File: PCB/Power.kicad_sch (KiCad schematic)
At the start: 18 parts, among them J2 USB-C, U4 USBLC6-2SC6, U8 AP2112K-3.3TRG1, U9 MP1584EN

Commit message: Power sheet P2: USB-C fix, buck replacement, LDO rewire, battery sense, pull-downs
- Replaced MP1584 buck with TPS54360 (EOL fix)
- Fixed USB-C: CC pull-downs, ESD wiring, VBUS path, shell ground
- Rewired LDO: VIN<-+5V, GND->GND, VOUT->+3V3, caps at pins
- Added battery sense divider (100k/10k from VBAT)
- Added SBU1/SBU2 1M pull-downs (R38, R39)
- Fixed component rotations for distinct pin tips (90°)
- Added PWR_FLAGS on +5V rail (source) and VBUS net
- Added SBU1/SBU2 1M pull-downs (R38, R39)
- Removed old MP1584 debris
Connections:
- net USB_D_P is gone; now on net GND: J2.A6 (DP1), J2.B6 (DP2), U4.1 (I/O1), U4.6 (I/O1)
- net GND: now also J2.A5 (CC1), J2.A8 (SBU1), J2.B5 (CC2); no longer R11.1, R4.2, R9.2
- net VBUS: now also R4.2
- net at R11.2: no longer J2.A5 (CC1)
- net at R4.1: no longer J2.B5 (CC2)
- net at R8.2, U9.4 (FB): no longer R9.1
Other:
- moved on the sheet: R11, R4, R9

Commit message: Hierarchy: Power sheet hierarchical labels + root sheet pins (via Konnect)
- Added 5 hierarchical labels to Power.kicad_sch (VBAT, USB_D_P, USB_D_N, VBUS_SENSE, VBUS_DIV)
- Imported matching sheet pins onto root Power instance
- validate_sheet_pins: 0 issues; both files parse cleanly
- Root cause of A1: sub-sheets had only local labels, zero hierarchical labels
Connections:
- net GND: no longer J2.A5 (CC1), J2.A6 (DP1), J2.A8 (SBU1), J2.B5 (CC2), J2.B6 (DP2), U4.1 (I/O1), U4.6 (I/O1)
- new net USB_D_P: J2.A6 (DP1), J2.B6 (DP2), U4.1 (I/O1), U4.6 (I/O1)

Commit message: Root cleanup: no_connect markers + VBAT/BARO_INT root nets + stale PWR_FLAG cleanup
- Added 42 no_connect markers to intentionally floating MCU pins
- Removed 3 stale PWR_FLAGS from root (SPI_CS_GYRO, BMI_INT3, SW)
- Added VBAT and BARO_INT hierarchical labels to root
- Added PWR_FLAGS on +5V rail source and VBUS net
- Hierarchy fully valid (validate_sheet_pins: 0 issues)
- Remaining ERC: root floating pins + power sheet residue + peripheral PWM block
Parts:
- removed C25: C0402C104K3RACTU, C0402C104K3RACTU:CAPC1005X55N, symbol C0402C104K3RACTU:C0402C104K3RACTU
- removed C4: C0402C104K3RACTU, C0402C104K3RACTU:CAPC1005X55N, symbol Device:C_Small
- removed R10, R25, R8: RC0402FR-07100KL, RC0402FR-07100KL:RESC1005X40, symbol Device:R
- added C50, C53: 100nF, symbol Device:C_Small
- added C51, C52: 10uF/50V, symbol Device:C_Small
- added C54: 5.6nF, symbol Device:C_Small
- added C55, C56: 22uF, symbol Device:C_Small
- added D1: SK34, symbol OpenVCU:SK34
- added L1: 10uH, symbol OpenVCU:L-10uH
- added R50: 442k, symbol Device:R
- added R51: 68.1k, symbol Device:R
- added R52: 196k, symbol Device:R
- added R53: 100k, symbol Device:R
- added R54: 19.1k, symbol Device:R
- added R55: 14k, symbol Device:R
- U9: value MP1584EN -> TPS54360; symbol MP1584EN:MP1584EN -> OpenVCU:TPS54360
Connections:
- net VBAT is gone; now on net GND: U9.7 (GND)
- net VBUS is gone; now on net GND: D1.2 (A), J2.A4B9 (VBUS), J2.B4A9 (VBUS), R4.2, R5.1, U4.5 (VBUS)
- net +5V: now also U9.8 (SW), C50.2, C55.1, C56.1, L1.1, L1.2, R53.1
- net GND: now also U9.2 (VIN), C51.1, C51.2, C52.1, C52.2, C53.1, C53.2, C54.2, C55.2, C56.2, R50.1, R51.2, R52.2, R54.2; no longer U9.5 (GND), U9.6 (FREQ)
- net RT: now reaches U9.4 (RT/CLK)
- net RT: now also R52.1
- net Comp_resistor renamed EN_DIV
- net EN_DIV: now also R50.2, R51.1
- net SW_NODE renamed BOOT_DRV
- net BOOT_DRV: now also C50.1
- new net COMP: R53.2, R54.1, R55.1, U9.5 (FB), U9.6 (COMP)
- new net COMP_C: C54.1, R55.2

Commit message: Power+root: drive every ERC error to zero
Power sheet
- add power:PWR_FLAG to the lib_symbols cache under its full lib_id so the
  flags actually resolve to a pin (a bare "PWR_FLAG" cache key resolves to
  zero pins and silently disables the flag)
- one PWR_FLAG per net: +5V, FB divider node, VBUS_SENSE
- name the TPS54360 divider node FB so R53/R54/R55 join U9.5's net
- wire U9.8 (SW) to the existing SW label (buck half-bridge)
- drop 12 orphan power symbols, the duplicate D_Schottky ref, R9/C28 and
  14 junk wires; re-point the USB-C CC pull-downs at Device:R
- rebuild the FB/COMP network to the standard TPS54360 divider
- label the USBLC6 pass-through pins USB_D_P/USB_D_N/VBUS_SENSE

Root sheet
- label NRST so the MCU reset net reaches the SWD header
- retarget C27 (NRST decoupling) from the oscillator rail to GND, with a real
  library symbol and footprint
- add PWR_FLAGs on GND, +3V3, VREF+, VCAP1 and VCAP2
- delete two dangling wire stubs

ERC: 240 errors -> 0.
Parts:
- removed C28: GRM1555C1H222JA01D, GRM1555C1H222JA01D:CAPC1005X55N, symbol GRM1555C1H222JA01D:GRM1555C1H222JA01D
- removed D1: D_Schottky, B5819W:SDO_SOD-123_MCC, symbol Device:D_Schottky
- removed R9: 20K Ohms, RC0402FR-0720KL:RESC1005X40N, symbol RC0402FR-0720KL:RC0402FR-0720KL
- added C34: 10nF, Capacitor_SMD:C_0402_1005Metric, symbol Device:C_Small
- R11, R4: value RC0402FR-075K1L -> 5.1k; footprint RC0402FR-075K1L:RESC1005X40N -> Resistor_SMD:R_0402_1005Metric; symbol RC0402FR-075K1L:RC0402FR-075K1L -> Device:R
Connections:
- net +5V: no longer C50.2, L1.1, U9.8 (SW)
- net COMP: now also C34.1; no longer R53.2, R54.1, R55.1, U9.5 (FB)
- net GND: now also D1.2 (A), R11.1, C34.2; no longer J2.A4B9 (VBUS), J2.B4A9 (VBUS), R5.1, U4.5 (VBUS)
- net at J2.A5 (CC1): now also R11.2
- net at J2.B5 (CC2): now also R4.1
- net SW: now reaches D1.1 (K)
- net SW: now also C50.2, L1.1, U9.8 (SW)
- new net FB: R53.2, R54.1, R55.1, U9.5 (FB)
- new net VBUS: J2.A4B9 (VBUS), J2.B4A9 (VBUS), R5.1, U4.5 (VBUS)
- no-connect marks 0 -> 2
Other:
- moved on the sheet: C54, R54, R55

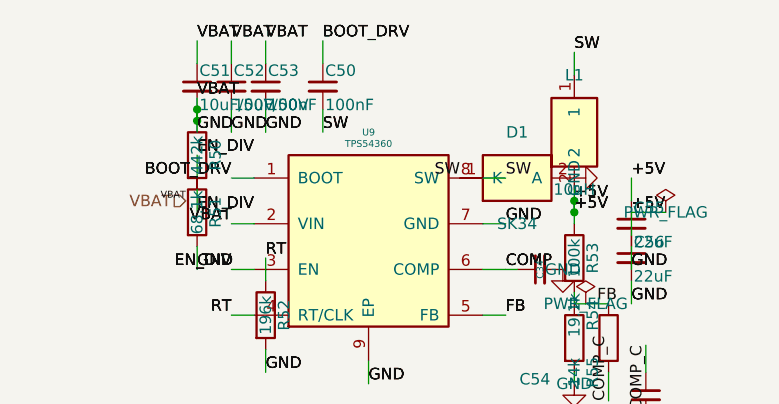
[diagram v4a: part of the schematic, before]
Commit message: Power: fix the shorted buck input rail (VBAT)
The buck input network was silently shorted to GND and had no VBAT net at all:

  * L1.1 (inductor, SW side) was wired to the +5V node instead of SW, shorting
    SW to +5V through the inductor
  * C51.2's GND stub passed straight through R50.1's pin, dragging the TPS54360
    feedback/EN divider top and VIN down to GND

Rebuild the VBAT tap and the +5V output node so that

  /Power/VBAT = C51.1, C52.1, C53.1, R50.1, U9.2 (VIN)
  /Power/SW   = C50.2, D1.1, L1.1, U9.8          (catch diode + inductor)
  +5V         = C55.1, C56.1, L1.2, R53.1, ...

Also drop the vestigial VBAT hierarchical pin (Power + Peripherals) and its two
root labels: nothing on the root or Peripherals sheets consumes battery voltage,
and the MCU VBAT pin is tied to +3V3 on the root, so it was dangling.
Add a PWR_FLAG on the VBAT rail.

New tools: /tmp/opencode/overlap.py and junctions.py detect collinear-overlap and
T-junction shorts, which ERC does not report.

ERC: 0 errors.
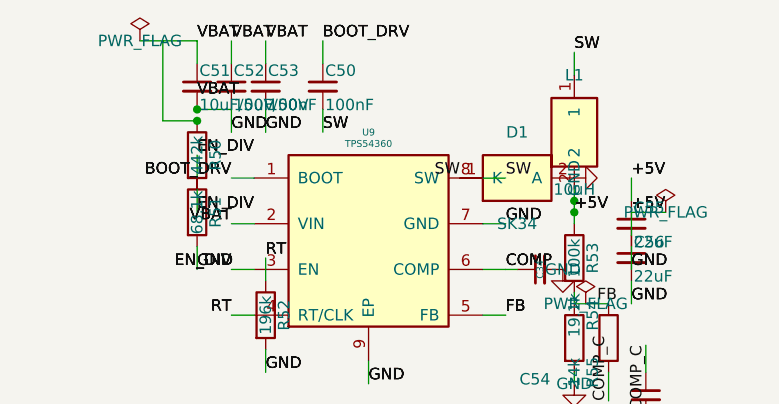
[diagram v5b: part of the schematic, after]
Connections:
- net GND: no longer C51.1, C52.1, C53.1, R50.1, U9.2 (VIN)
- new net VBAT: C51.1, C52.1, C53.1, R50.1, U9.2 (VIN)
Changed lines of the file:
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@@
 	(wire
 		(pts
-			(xy 38.1 22.86)
-			(xy 38.1 25.4)
-		)
-	)
-	(wire
-		(pts
 			(xy 41.91 17.78)
 			(xy 41.91 15.24)
@@
 	(wire
 		(pts
-			(xy 38.1 24.13)
-			(xy 38.1 21.59)
-		)
-	)
-	(wire
-		(pts
 			(xy 38.1 31.75)
 			(xy 38.1 34.29)
@@
 	(wire
 		(pts
-			(xy 80.01 35.56)
-			(xy 80.01 33.02)
-		)
-	)
-	(wire
-		(pts
-			(xy 80.01 19.05)
-			(xy 80.01 16.51)
-		)
-	)
-	(wire
-		(pts
-			(xy 80.01 31.75)
-			(xy 80.01 34.29)
-		)
-	)
-	(wire
-		(pts
 			(xy 86.36 33.02)
 			(xy 86.36 30.48)
@@
 		)
 	)
-	(label "VBAT"
-		(at 36.83 33.02 180)
-		(effects
-			(font
-				(size 0.762 0.762)
-			)
-			(justify right bottom)
-		)
-	)
 	(label "BOOT_DRV"
 		(at 41.91 30.48 180)
@@
 		)
 	)
-	(label "GND"
-		(at 38.1 25.4 0)
-		(effects
-			(font
-				(size 1.27 1.27)
-			)
-			(justify left bottom)
-		)
-	)
 	(label "VBAT"
 		(at 41.91 15.24 0)
@@
 		)
 	)
-	(label "+5V"
-		(at 80.01 33.02 0)
-		(effects
-			(font
-				(size 1.27 1.27)
-			)
-			(justify left bottom)
-		)
-	)
 	(label "SW"
 		(at 80.01 16.51 0)
@@
 		)
 	)
-	(label "GND"
-		(at 38.1 25.4 0)
-		(effects
-			(font
-				(size 1.27 1.27)
-			)
-			(justify left bottom)
-		)
-	)
 	(label "VBAT"
 		(at 41.91 15.24 0)
@@
 		)
 	)
-	(label "+5V"
-		(at 80.01 33.02 0)
-		(effects
-			(font
-				(size 1.27 1.27)
-			)
-			(justify left bottom)
-		)
-	)
 	(label "SW"
 		(at 80.01 16.51 0)
@@
 		)
 	)
-	(hierarchical_label "VBAT"
-		(shape input)
-		(at 36.83 33.02 180)
-		(effects
-			(font
-				(size 1.27 1.27)
-			)
-			(justify right)
-		)
-	)
 	(symbol
 		(lib_id "power:+5V")
@@
 		)
 	)
+	(wire
+		(pts
+			(xy 38.1 22.86)
+			(xy 41.91 22.86)
+		)
+		(stroke
+			(width 0)
+			(type default)
+		)
+	)
+	(wire
+		(pts
+			(xy 38.1 24.13)
+			(xy 34.29 24.13)
+		)
+		(stroke
+			(width 0)
+			(type default)
+		)
+	)
+	(wire
+		(pts
+			(xy 34.29 24.13)
+			(xy 34.29 15.24)
+		)
+		(stroke
+			(width 0)
+			(type default)
+		)
+	)
+	(wire
+		(pts
+			(xy 34.29 15.24)
+			(xy 38.1 15.24)
+		)
+		(stroke
+			(width 0)
+			(type default)
+		)
+	)
+	(wire
+		(pts
+			(xy 80.01 19.05)
+			(xy 80.01 16.51)
+		)
+		(stroke
+			(width 0)
+			(type default)
+		)
+	)
+	(wire
+		(pts
+			(xy 80.01 31.75)
+			(xy 80.01 35.56)
+		)
+		(stroke
+			(width 0)
+			(type default)
+		)
+	)
+	(wire
+		(pts
+			(xy 34.29 15.24)
+			(xy 31.75 15.24)
+		)
+		(stroke
+			(width 0)
+			(type default)
+		)
+	)
+	(symbol
+		(lib_id "power:PWR_FLAG")
+		(at 31.75 15.24 0)
+		(unit 1)
+		(exclude_from_sim no)
+		(in_bom yes)
+		(on_board yes)
+		(dnp no)
+		(property "Reference" "#FLG0203"
+			(at 31.75 15.24 0)
+			(hide yes)
+			(show_name no)
+			(do_not_autoplace no)
+			(effects
+				(font
+					(size 0.762 0.762)
+				)
+			)
+		)
+		(property "Value" "PWR_FLAG"
+			(at 31.75 15.24 0)
+			(do_not_autoplace no)
+			(effects
+				(font
+					(size 1.27 1.27)
+				)
+			)
+		)
+		(property "Footprint" ""
+			(at 31.75 15.24 0)
+			(hide yes)
+			(show_name no)
+			(do_not_autoplace no)
+			(effects
+				(font
+					(size 1.27 1.27)
+				)
+			)
+		)
+		(property "Datasheet" ""
+			(at 31.75 15.24 0)
+			(hide yes)
+			(show_name no)
+			(do_not_autoplace no)
+			(effects
+				(font
+					(size 1.27 1.27)
+				)
+			)
+		)
+		(property "Description" "Power flag"
+			(at 31.75 15.24 0)
+			(hide yes)
+			(show_name no)
+			(do_not_autoplace no)
+			(effects
+				(font
+					(size 1.27 1.27)
+				)
+			)
+		)
+		(in_pos_files yes)
+		(pin "1"
+		)
+		(instances
+			(project "OpenVCU"
+				(path "/aca1b137-7238-4712-8ae7-b508bd275e0a/02d77783-822b-4912-9c40-908f263f3588"
+					(reference "#FLG0203")
+					(unit 1)
+				)
+			)
+		)
+	)

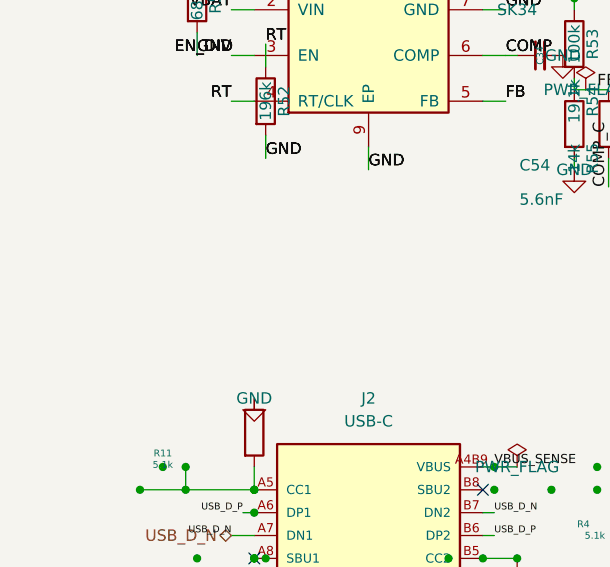
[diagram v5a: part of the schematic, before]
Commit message: Power: add battery input stage (J12, F1, D2)
2S-4S Li-ion (7.4-16.8 V) feed for the TPS54360 buck:

  J12  OpenVCU:PADROW-2        battery connector (+/-)
  F1   Device:Fuse / 5A        fuse, 1206
  D2   Device:D_TVS / SMBJ18A  bidirectional TVS to GND, SMB
  C51-C53                      3x 10uF/50V bulk on the VBAT rail

Net /Power/VBAT = J12(via F1), D2, C51/C52/C53, R50 divider, U9 VIN.
Also fix libsync's project-library parser (the project .kicad_sym stores
symbols at a different indentation) and normalise inserted cache entries to
carry the full lib_id as the key.

ERC: 0 errors.
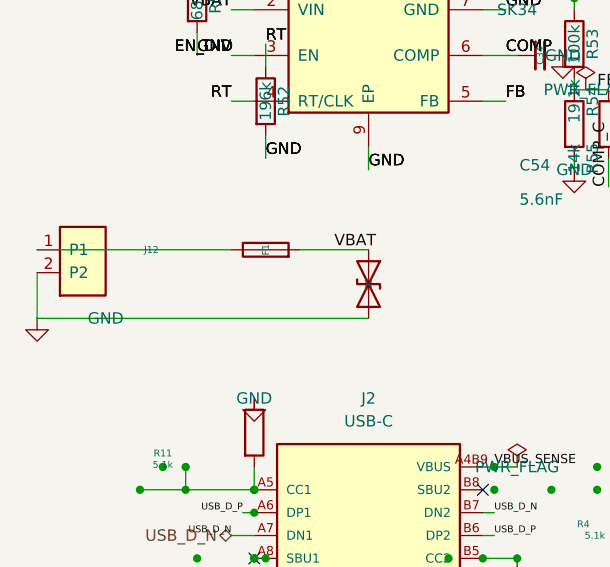
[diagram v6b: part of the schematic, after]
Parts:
- added D2: SMBJ18A, Diode_SMD:D_SMB, symbol Device:D_TVS
- added F1: 5A, Fuse:Fuse_1206_3216Metric, symbol Device:Fuse
- added J12: PADROW-2, OpenVCU:PADROW-2, symbol OpenVCU:CONN-2
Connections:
- net GND: now also D2.2 (A2), J12.2 (P2)
- net VBAT: now also D2.1 (A1), F1.2
- new net: F1.1, J12.1 (P1)

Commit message: Power/root: fix USB VBUS sensing and remove ambiguous net names
  * U1.68 (PA9) was wired straight to raw VBUS, so the MCU saw up to 20V
    instead of the divided voltage. It is now on VBUS_DIV, whose only other
    members are the R1/R5 divider tap and U1.15 (PC0)
  * the divider's top node is labelled VBUS, matching the USB-C VBUS pins and
    the USBLC6 VBUS pin, so there is no VBUS/VBUS_SENSE clash
  * drop the now-unused VBUS_SENSE hierarchical pin and its root label

ERC: 0 errors, 201 -> 190 warnings.
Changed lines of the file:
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@@
 		)
 	)
-	(label "VBUS_SENSE"
-		(at 34.29 170.18 180)
-		(effects
-			(font
-				(size 1.016 1.016)
-			)
-			(justify right bottom)
-		)
-	)
 	(label "USB_D_N"
 		(at 71.12 91.44 0)
@@
 		)
 	)
-	(label "VBUS_SENSE"
-		(at 71.12 86.36 0)
-		(effects
-			(font
-				(size 1.016 1.016)
-			)
-			(justify left bottom)
-		)
-	)
 	(label "USB_D_N"
 		(at 39.37 177.8 0)
@@
 		)
 	)
-	(label "VBUS_SENSE"
-		(at 58.42 173.99 180)
-		(effects
-			(font
-				(size 1.016 1.016)
-			)
-			(justify right bottom)
-		)
-	)
 	(label "BOOT_DRV"
 		(at 41.91 30.48 180)
@@
 		)
 	)
-	(hierarchical_label "VBUS_SENSE"
-		(shape output)
-		(at 34.29 170.18 180)
-		(effects
-			(font
-				(size 1.27 1.27)
-			)
-			(justify right)
-		)
-	)
 	(hierarchical_label "VBUS_DIV"
 		(shape output)
@@
 		)
 	)
+	(label "VBUS"
+		(at 58.42 173.99 180)
+		(effects
+			(font
+				(size 1.27 1.27)
+			)
+			(justify right bottom)
+		)
+	)
+	(label "VBUS"
+		(at 34.29 170.18 180)
+		(effects
+			(font
+				(size 1.27 1.27)
+			)
+			(justify right bottom)
+		)
+	)
+	(label "VBUS"
+		(at 71.12 86.36 0)
+		(effects
+			(font
+				(size 1.27 1.27)
+			)
+			(justify left bottom)
+		)
+	)
